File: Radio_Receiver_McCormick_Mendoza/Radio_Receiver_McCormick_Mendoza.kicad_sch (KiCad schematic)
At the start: 17 parts, among them J43 Conn_01x02, J44 Conn_01x02

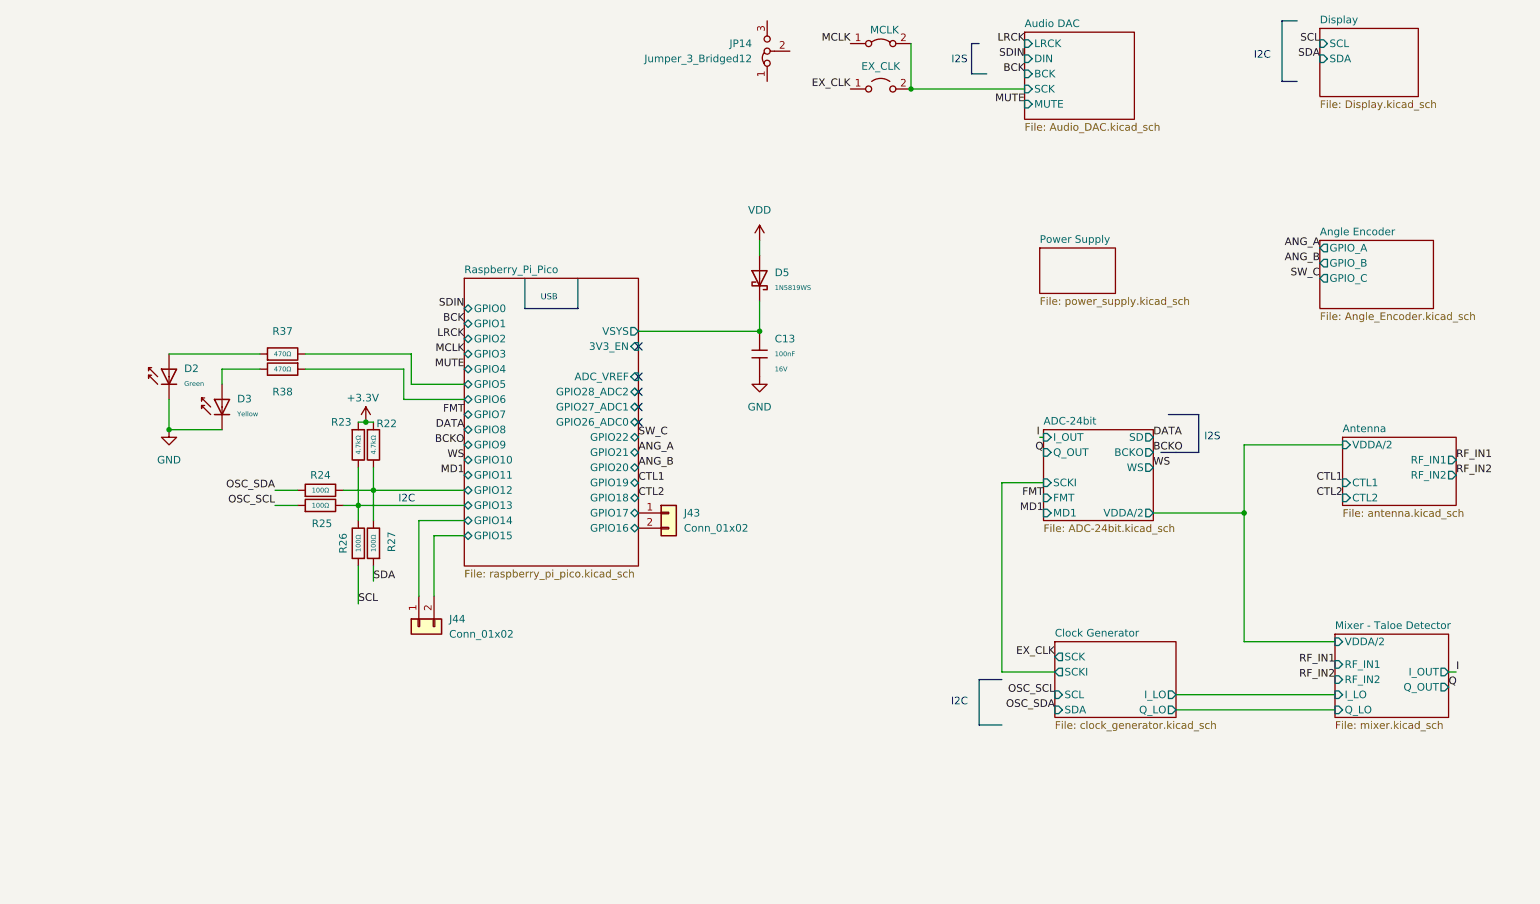
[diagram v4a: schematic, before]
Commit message: Added MicroSD card and verified footprints
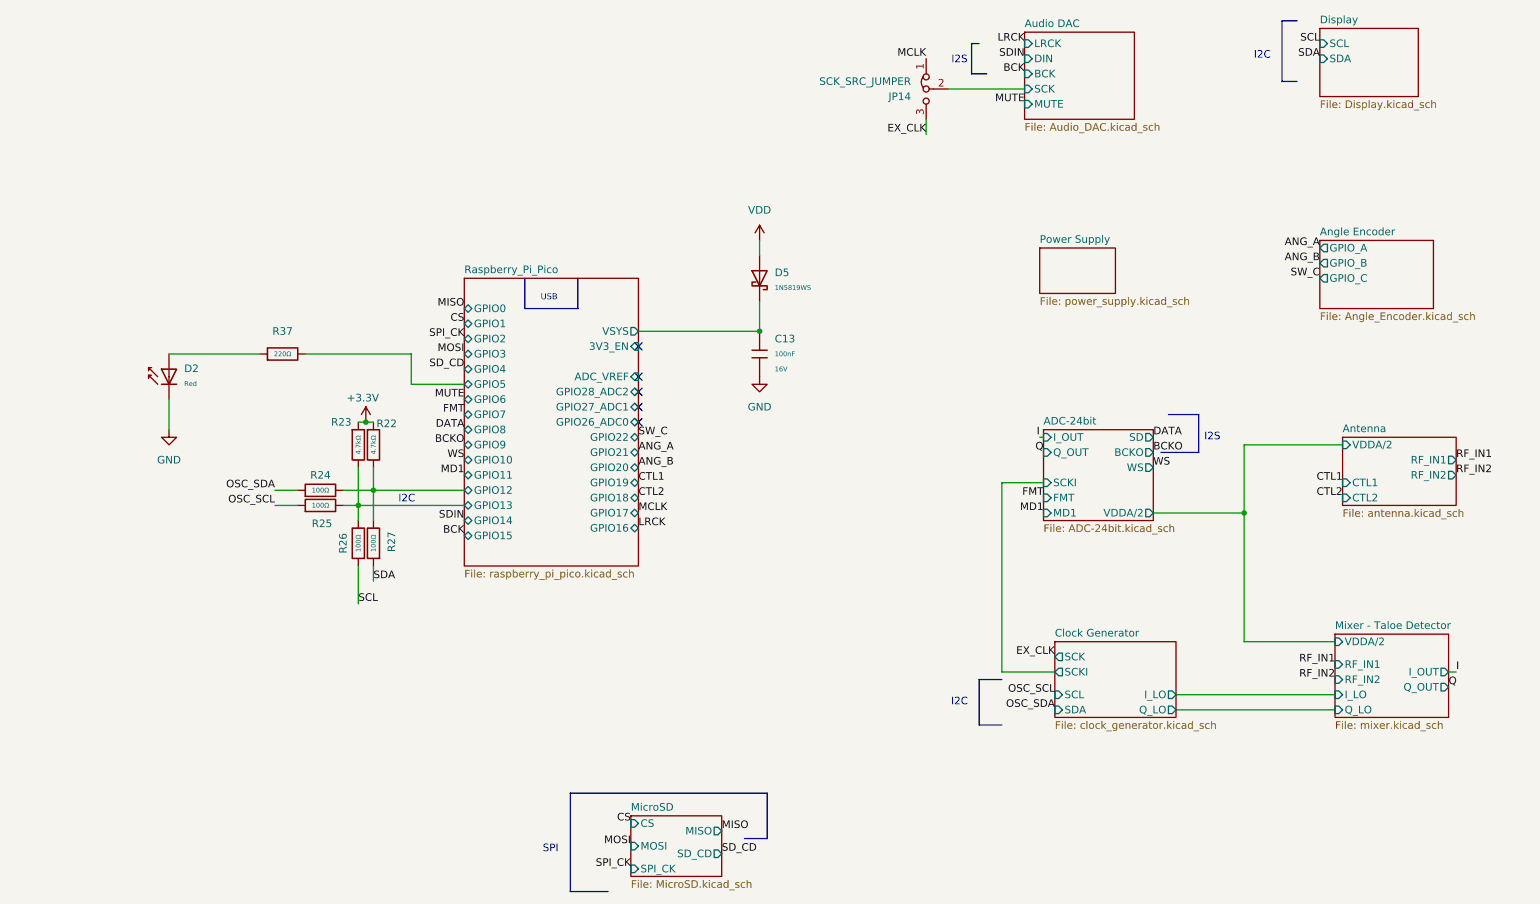
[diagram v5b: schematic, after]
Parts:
- removed D2: Green, PCM_JLCPCB:D_0805, symbol PCM_JLCPCB-Diodes:LED,0805,Green
- removed D3: Yellow, PCM_JLCPCB:D_0805, symbol PCM_JLCPCB-Diodes:LED,0805,Yellow
- removed J43, J44: Conn_01x02, Connector_PinHeader_2.54mm:PinHeader_1x02_P2.54mm_Vertical, symbol Connector_Generic:Conn_01x02
- removed JP13: EX_CLK, Jumper:SolderJumper-2_P1.3mm_Open_RoundedPad1.0x1.5mm, symbol Jumper:Jumper_2_Open
- removed R37, R38: 470Ω, PCM_JLCPCB:R_0603, symbol PCM_JLCPCB-Resistors:0603,470Ω
- removed e9: MCLK, Jumper:SolderJumper-2_P1.3mm_Bridged_RoundedPad1.0x1.5mm, symbol Jumper:Jumper_2_Bridged
- added D2: Red, PCM_JLCPCB:D_0805, symbol PCM_JLCPCB-Diodes:LED,0805,Red
- added R37: 220Ω, PCM_JLCPCB:R_0603, symbol PCM_JLCPCB-Resistors:0603,220Ω
- D5: Manufacturer Guangdong Hottech -> (none)
- JP14: value Jumper_3_Bridged12 -> SCK_SRC_JUMPER; footprint (none) -> Jumper:SolderJumper-3_P1.3mm_Bridged2Bar12_RoundedPad1.0x1.5mm_NumberLabels; now in the parts list
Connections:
- net Audio DAC/SCK: now also JP14.2 (C)
- net EX_CLK: now also JP14.3 (B)
- net GND: now also D2.1
- net MCLK: now also JP14.1 (A)
- net Raspberry_Pi_Pico/GPIO5: now also R37.2
- new net: D2.2, R37.1
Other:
- added sheet MicroSD (MicroSD.kicad_sch)
- note added: "SPI"
- moved on the sheet: JP14

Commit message: Routed antenna and isolated GNDA
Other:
- sheet ADC-24bit ports: added VREF; removed VDDA/2
- sheet Antenna ports: added VREF; removed VDDA/2
- sheet Mixer - Taloe Detector ports: added VREF; removed VDDA/2
- moved on the sheet: D2, R37
